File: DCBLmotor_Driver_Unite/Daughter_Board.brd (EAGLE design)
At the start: 107.5 x 78.7 mm, 64 parts, among them CN1 DF11-16DP-2DSA, CN2 26-01-3115, CN3 39-28-1023, IC1 ACS780KLRTR-150B-T, IC2 IR2010SPBF, IC3 IR2010SPBF, IC4 IR2010SPBF, IC5 ACS780KLRTR-150B-T, IC6 ACS780KLRTR-150B-T

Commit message: Version1 per finshed
Per complete Version1
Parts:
- added CN4: (no value), jst-xh:B2B-XH-A
- added PMC4: 50ST104MA13216, Rubycon:3216
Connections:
- new net N$31: DC-DC1.P$6, PMC4.P$1
- net +20V: now also CN4.1
- net GND: now also CN4.2, PMC4.P$2
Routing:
- net GND: track 439.8 -> 447.6 mm
- net CU1: track 60.3 -> 65.8 mm
- net N$31: track 0.00 -> 1.83 mm
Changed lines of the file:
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@@
 <element name="R8" library="ROHM" package="MCR03" value="MCR03" x="88.62554375" y="15.636859375" rot="R180"/>
 <element name="D1" library="DIODE" package="SOD123" value="1N5711W-7-F" x="81.7" y="16.5" rot="R180"/>
+<element name="PMC4" library="Rubycon" package="3216" value="50ST104MA13216" x="89.5" y="19.8"/>
+<element name="CN4" library="jst-xh" package="B2B-XH-A" value="" x="0.8" y="-4.4"/>
 </elements>
 <signals>
@@
 <wire x1="90.099634375" y1="29.800365625" x2="87.4" y2="32.5" width="3" layer="1"/>
 <wire x1="84.8" y1="13.3" x2="92.9" y2="13.3" width="3" layer="1"/>
-<wire x1="96.917065625" y1="17.317065625" x2="96.917065625" y2="23.163078125" width="3" layer="1"/>
+<wire x1="96.917065625" y1="17.317065625" x2="96.917065625" y2="19.8" width="3" layer="1"/>
+<wire x1="96.917065625" y1="19.8" x2="96.917065625" y2="23.163078125" width="3" layer="1"/>
 <wire x1="92.9" y1="13.3" x2="96.917065625" y2="17.317065625" width="3" layer="1"/>
 <wire x1="96.917065625" y1="23.163078125" x2="92.590071875" y2="27.490071875" width="3" layer="1"/>
@@
 <wire x1="84.279053125" y1="30.466625" x2="87.25560625" y2="27.490071875" width="3" layer="1"/>
 <wire x1="87.25560625" y1="27.490071875" x2="92.590071875" y2="27.490071875" width="3" layer="1"/>
+<contactref element="PMC4" pad="P$2"/>
+<wire x1="92.7" y1="19.8" x2="94.9" y2="19.8" width="1.016" layer="1"/>
+<wire x1="94.9" y1="19.8" x2="96.917065625" y2="19.8" width="1.016" layer="1"/>
+<wire x1="94.9" y1="19.8" x2="96.2" y2="18.5" width="1.016" layer="1"/>
+<wire x1="94.9" y1="19.8" x2="96.1" y2="21" width="1.016" layer="1"/>
+<contactref element="CN4" pad="2"/>
 <wire x1="25.7" y1="66.472175" x2="25.814715625" y2="66.76835" width="0" layer="19" extent="16-16"/>
 <wire x1="25.618125" y1="33.3421125" x2="25.618125" y2="33.342115625" width="0" layer="19" extent="16-16"/>
+<wire x1="2.05" y1="-4.4" x2="19.5" y2="20.3" width="0" layer="19" extent="16-16"/>
 </signal>
 <signal name="N$1">
@@
 <wire x1="18.3" y1="37.2" x2="15.4" y2="34.3" width="0.2" layer="1"/>
 <wire x1="13.9" y1="34.3" x2="15.4" y2="34.3" width="0.2" layer="1"/>
-<wire x1="7.6" y1="31.5" x2="9.1" y2="33" width="0.15" layer="1"/>
-<wire x1="9.1" y1="33" x2="12.5" y2="33" width="0.15" layer="1"/>
-<wire x1="12.5" y1="33" x2="13.8" y2="34.3" width="0.15" layer="1"/>
-<wire x1="13.8" y1="34.3" x2="13.9" y2="34.3" width="0.15" layer="1"/>
+<wire x1="7.65" y1="31.55" x2="9.1" y2="33" width="0.15" layer="1"/>
+<wire x1="13.9" y1="34.3" x2="13.8" y2="34.3" width="0.15" layer="1"/>
+<wire x1="7.6" y1="31.5" x2="7.65" y2="31.55" width="0.1524" layer="1"/>
+<wire x1="13.9" y1="34.3" x2="10.4" y2="34.3" width="0.1524" layer="1"/>
+<wire x1="13.8" y1="34.3" x2="10.4" y2="34.3" width="0.2" layer="1"/>
+<wire x1="10.4" y1="34.3" x2="7.65" y2="31.55" width="0.2" layer="1"/>
 <wire x1="29.709803125" y1="71.00635" x2="29.709815625" y2="71.006359375" width="0" layer="19" extent="16-16"/>
 </signal>
@@
 <wire x1="90.099634375" y1="44.531209375" x2="90.099634375" y2="48.900365625" width="3" layer="1"/>
 <wire x1="90.099634375" y1="48.900365625" x2="85.9" y2="53.1" width="3" layer="1"/>
+<contactref element="CN4" pad="1"/>
+<wire x1="-0.45" y1="-4.4" x2="70.5" y2="28.7" width="0" layer="19" extent="16-16"/>
 </signal>
 <signal name="VCC">
@@
 <wire x1="85.840809375" y1="16.614103125" x2="85.840809375" y2="16.61410625" width="0" layer="19" extent="1-1"/>
 </signal>
+<signal name="N$31">
+<contactref element="DC-DC1" pad="P$6"/>
+<contactref element="PMC4" pad="P$1"/>
+<wire x1="89.5" y1="19.8" x2="87.712428125" y2="19.8" width="1.016" layer="1"/>
+<wire x1="87.712428125" y1="19.8" x2="87.679053125" y2="19.766625" width="1.016" layer="1"/>
+</signal>
 </signals>

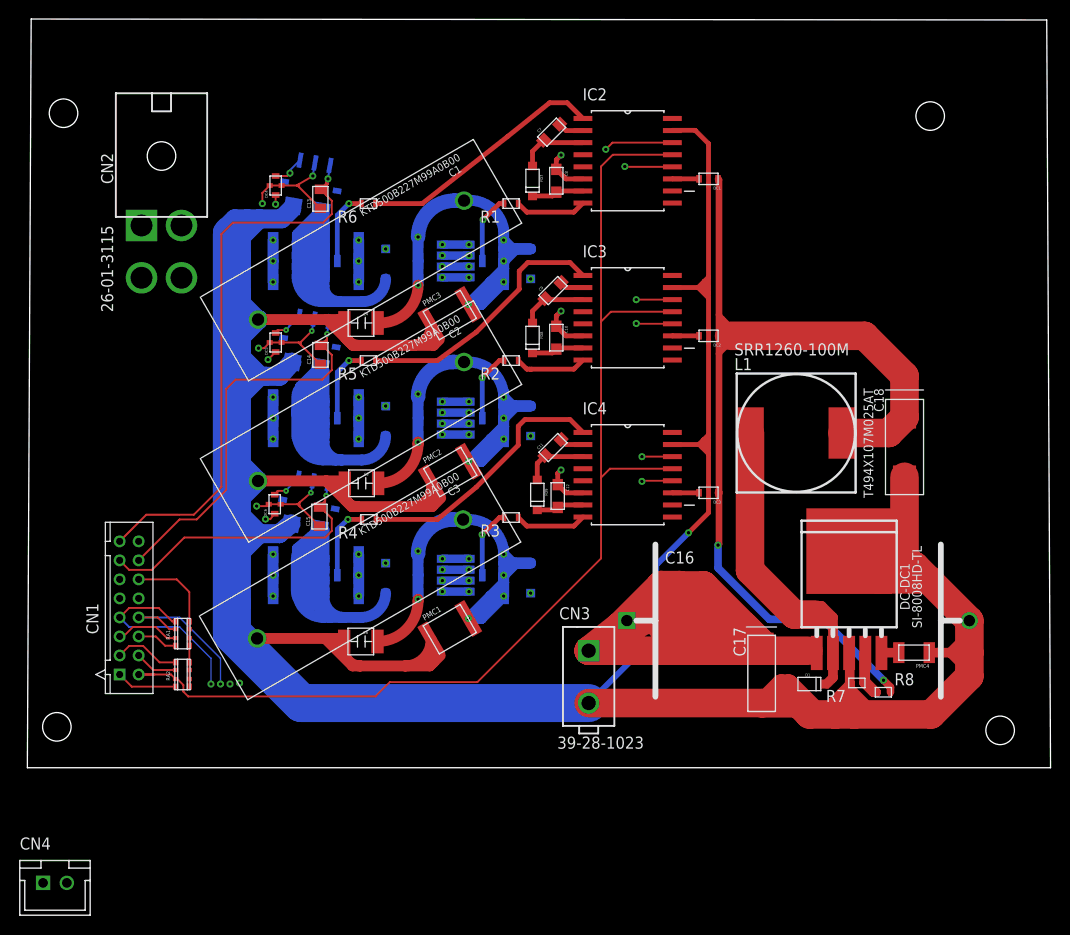
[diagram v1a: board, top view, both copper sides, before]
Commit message: Fix
Add coment in silk
rerote some line
fix External form
Add screw hole
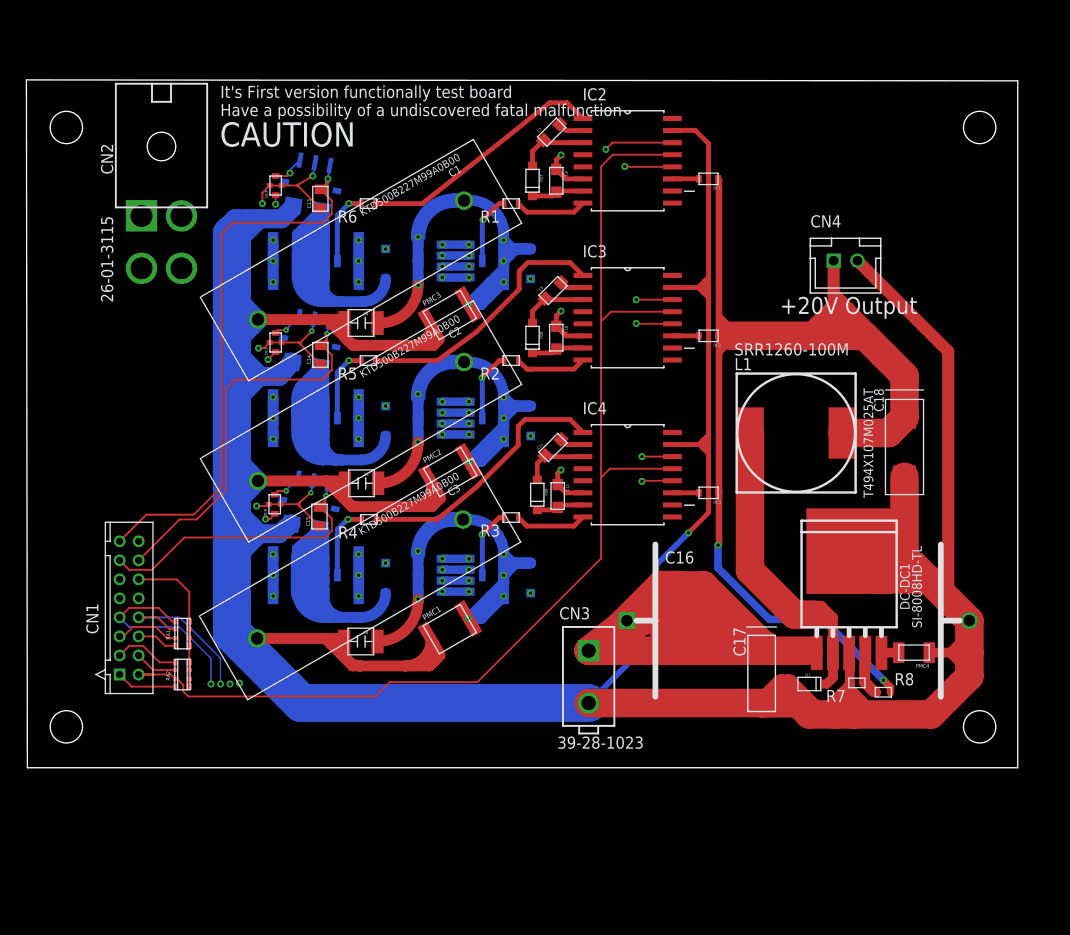
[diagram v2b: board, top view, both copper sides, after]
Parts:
- moved CN4 105.7 mm to (83.9, 61.0)
- moved CN2 1.00 mm to (12.0, 65.7)
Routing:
- net GND: track 447.6 -> 490.3 mm
- net +20V: track 104.1 -> 135.4 mm
- net VS2: track 111.6 -> 112.6 mm
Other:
- board size 107.5 x 78.7 mm -> 104.2 x 72.3 mm
- board text added: "+20V Output"
- board text added: "CAUTION"
- board text added: "It's First version functionally test board Have a possibility of a undiscovered fatal malfunction"
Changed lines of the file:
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@@
 <setting verticaltext="up"/>
 </settings>
-<grid distance="0.1" unitdist="mm" unit="mm" style="lines" multiple="1" display="no" altdistance="5" altunitdist="mil" altunit="mm"/>
+<grid distance="1" unitdist="mm" unit="mm" style="lines" multiple="1" display="no" altdistance="5" altunitdist="mil" altunit="mm"/>
 <layers>
 <layer number="1" name="Top" color="4" fill="1" visible="yes" active="yes"/>
@@
 <board>
 <plain>
-<wire x1="-2.1" y1="7.7" x2="105.45" y2="7.7" width="0" layer="20"/>
-<wire x1="105.45" y1="7.7" x2="105.05" y2="86.3" width="0" layer="20"/>
-<wire x1="105.05" y1="86.3" x2="-1.7" y2="86.4" width="0" layer="20"/>
-<wire x1="-1.7" y1="86.4" x2="-2.1" y2="7.7" width="0" layer="20"/>
-<hole x="1.7" y="76.5" drill="3"/>
-<hole x="92.8" y="76.2" drill="3"/>
-<hole x="100.15179375" y="11.63115" drill="3"/>
-<hole x="1" y="12" drill="3"/>
-<dimension x1="-2.1" y1="7.7" x2="105.45" y2="7.7" x3="51.675" y3="83.4" textsize="1.778" layer="1"/>
-<dimension x1="1" y1="74.9" x2="3.8" y2="7.8" x3="-4.74835625" y3="41.051709375" textsize="1.778" layer="1"/>
+<wire x1="-2.1" y1="7.7" x2="102" y2="7.7" width="0" layer="20"/>
+<wire x1="102" y1="7.7" x2="102" y2="79.9" width="0" layer="20"/>
+<wire x1="102" y1="79.9" x2="-2.2" y2="80" width="0" layer="20"/>
+<wire x1="-2.2" y1="80" x2="-2.1" y2="7.7" width="0" layer="20"/>
+<text x="77" y="55.4" size="1.778" layer="21">+20V Output</text>
+<text x="52.525" y="12.2" size="1.27" layer="22" rot="MR0">It's First version functionally test board
+Have a possibility of a undiscovered fatal malfunction</text>
+<text x="52.575" y="9" size="2.54" layer="22" rot="MR0">CAUTION</text>
+<text x="18.175" y="76.2" size="1.27" layer="21">It's First version functionally test board
+Have a possibility of a undiscovered fatal malfunction</text>
+<text x="18.125" y="73" size="2.54" layer="21">CAUTION</text>
+<hole x="2" y="12" drill="3.4"/>
+<hole x="2" y="75" drill="3.4"/>
+<hole x="98" y="75" drill="3.4"/>
+<hole x="98" y="12" drill="3.4"/>
 </plain>
 <attributes>
@@
 <element name="RA1" library="Pana_Chip_RA" package="EXB-38V,28V" value="EXB-38V103JV" x="14.2" y="21.8" rot="R90"/>
 <element name="RA2" library="Pana_Chip_RA" package="EXB-38V,28V" value="EXB-38V103JV" x="14.2" y="17.5" rot="R90"/>
-<element name="CN2" library="Molex" package="26-01-3115" value="26-01-3115" x="12" y="64.7" rot="R180"/>
+<element name="CN2" library="Molex" package="26-01-3115" value="26-01-3115" x="12" y="65.7" rot="R180"/>
 <element name="CN3" library="Molex" package="39-28-1023" value="39-28-1023" x="56.9" y="20"/>
 <element name="DC-DC1" library="SANKEN" package="D2_PACAGE_5PIN" value="SI-8008HD-TL" x="84.279053125" y="27.466625"/>
@@
 <element name="D1" library="DIODE" package="SOD123" value="1N5711W-7-F" x="81.7" y="16.5" rot="R180"/>
 <element name="PMC4" library="Rubycon" package="3216" value="50ST104MA13216" x="89.5" y="19.8"/>
-<element name="CN4" library="jst-xh" package="B2B-XH-A" value="" x="0.8" y="-4.4"/>
+<element name="CN4" library="jst-xh" package="B2B-XH-A" value="" x="83.9" y="61"/>
 </elements>
 <signals>
@@
 <wire x1="94.9" y1="19.8" x2="96.1" y2="21" width="1.016" layer="1"/>
 <contactref element="CN4" pad="2"/>
+<wire x1="85.15" y1="61" x2="94.7" y2="51.45" width="1.27" layer="1"/>
+<wire x1="94.7" y1="25.38014375" x2="96.917065625" y2="23.163078125" width="1.27" layer="1"/>
+<wire x1="94.7" y1="51.45" x2="94.7" y2="25.38014375" width="1.27" layer="1"/>
 <wire x1="25.7" y1="66.472175" x2="25.814715625" y2="66.76835" width="0" layer="19" extent="16-16"/>
 <wire x1="25.618125" y1="33.3421125" x2="25.618125" y2="33.342115625" width="0" layer="19" extent="16-16"/>
-<wire x1="2.05" y1="-4.4" x2="19.5" y2="20.3" width="0" layer="19" extent="16-16"/>
 </signal>
 <signal name="N$1">
@@
 <wire x1="20.2" y1="60.9" x2="23.67" y2="60.9" width="4" layer="3"/>
 <wire x1="23.67" y1="60.9" x2="23.73" y2="60.96" width="4" layer="3"/>
-<wire x1="14.1" y1="64.7" x2="16.4" y2="64.7" width="3.5" layer="3"/>
+<wire x1="14.1" y1="65.7" x2="16.4" y2="64.7" width="3.5" layer="3"/>
 <wire x1="53.499996875" y1="70.6" x2="53.5" y2="70.6" width="0" layer="19" extent="1-1"/>
 </signal>
@@
 <wire x1="9.9" y1="57.3" x2="22.75" y2="44.45" width="4" layer="3"/>
 <wire x1="22.75" y1="44.45" x2="23.73" y2="44.45" width="4" layer="3"/>
-<wire x1="9.9" y1="59.2" x2="9.9" y2="57.3" width="3.5" layer="3"/>
+<wire x1="9.9" y1="60.2" x2="9.9" y2="57.3" width="3.5" layer="3"/>
 </signal>
 <signal name="VS3">
@@
 <wire x1="54" y1="29.26" x2="50.8" y2="26.06" width="0.508" layer="3"/>
 <contactref element="CN2" pad="P$1"/>
-<wire x1="9.9" y1="64.7" x2="8.7" y2="64.7" width="3.5" layer="3"/>
+<wire x1="9.9" y1="65.7" x2="8.7" y2="64.7" width="3.5" layer="3"/>
 <wire x1="5.2" y1="54.7" x2="17.6" y2="42.3" width="4" layer="3"/>
 <wire x1="17.6" y1="42.3" x2="17.6" y2="34.07" width="4" layer="3"/>
@@
 <wire x1="71" y1="54.9" x2="71" y2="53.9" width="0.508" layer="1"/>
 <wire x1="71" y1="53.9" x2="71.8" y2="53.1" width="0.508" layer="1"/>
-<wire x1="85.9" y1="53.1" x2="71.8" y2="53.1" width="3" layer="1"/>
+<wire x1="85.9" y1="53.1" x2="83.4" y2="53.1" width="3" layer="1"/>
 <contactref element="C18" pad="P$+"/>
+<wire x1="83.4" y1="53.1" x2="81.1" y2="53.1" width="3" layer="1"/>
+<wire x1="81.1" y1="53.1" x2="71.8" y2="53.1" width="3" layer="1"/>
 <wire x1="83.55994375" y1="42.88495625" x2="88.45338125" y2="42.88495625" width="3" layer="1"/>
 <wire x1="88.45338125" y1="42.88495625" x2="90.099634375" y2="44.531209375" width="3" layer="1"/>
 <wire x1="90.099634375" y1="44.531209375" x2="90.099634375" y2="48.900365625" width="3" layer="1"/>
-<wire x1="90.099634375" y1="48.900365625" x2="85.9" y2="53.1" width="3" layer="1"/>
+<wire x1="90.099634375" y1="48.900365625" x2="88.05" y2="50.95" width="3" layer="1"/>
 <contactref element="CN4" pad="1"/>
-<wire x1="-0.45" y1="-4.4" x2="70.5" y2="28.7" width="0" layer="19" extent="16-16"/>
+<wire x1="88.05" y1="50.95" x2="85.9" y2="53.1" width="3" layer="1"/>
+<wire x1="82.65" y1="61" x2="82.65" y2="57.55" width="1.27" layer="1"/>
+<wire x1="82.65" y1="57.55" x2="83.55" y2="56.65" width="1.27" layer="1"/>
+<wire x1="83.55" y1="56.65" x2="84.15" y2="56.05" width="1.27" layer="1"/>
+<wire x1="84.15" y1="56.05" x2="87.3" y2="52.9" width="1.27" layer="1"/>
+<wire x1="87.3" y1="52.9" x2="87.3" y2="50.8" width="1.27" layer="1"/>
+<wire x1="88.1" y1="50" x2="87.3" y2="50.8" width="1.27" layer="1"/>
+<wire x1="88.05" y1="50.95" x2="88.1" y2="50.9" width="1.27" layer="1"/>
+<wire x1="88.1" y1="50.9" x2="88.1" y2="50" width="1.27" layer="1"/>
+<wire x1="85.9" y1="53.1" x2="84.15" y2="54.85" width="1.27" layer="1"/>
+<wire x1="84.15" y1="54.85" x2="84.15" y2="56.05" width="1.27" layer="1"/>
+<wire x1="83.4" y1="53.1" x2="83.4" y2="56.5" width="1.27" layer="1"/>
+<wire x1="83.4" y1="56.5" x2="83.55" y2="56.65" width="1.27" layer="1"/>
+<wire x1="82.65" y1="57.55" x2="82.65" y2="56.4" width="1.27" layer="1"/>
+<wire x1="82.65" y1="56.4" x2="82.65" y2="54.7" width="1.27" layer="1"/>
+<wire x1="82.65" y1="54.65" x2="82.65" y2="53.95" width="1.27" layer="1"/>
+<wire x1="82.65" y1="53.95" x2="82.5" y2="53.8" width="1.27" layer="1"/>
+<wire x1="82.65" y1="56.4" x2="80" y2="53.75" width="1.27" layer="1"/>
+<wire x1="80" y1="53.75" x2="80" y2="53.7" width="1.27" layer="1"/>
+<wire x1="81.1" y1="53.1" x2="82.65" y2="54.65" width="1.27" layer="1"/>
+<wire x1="82.65" y1="54.65" x2="82.65" y2="54.7" width="1.27" layer="1"/>
 </signal>
 <signal name="VCC">
@@
 </board>
 </drawing>
+<compatibility>
+<note version="6.3" minversion="6.2.2" severity="warning">
+Since Version 6.2.2 text objects can contain more than one line,
+which will not be processed correctly with this version.
+</note>
+</compatibility>
 </eagle>

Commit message: Assigned Parts No.
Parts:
- added R10, R11, R12, R13, R14, R9: ESR03EZPJ753, ROHM:ESR03
- DC1, DC2, DC3, DC4, DC5, DC6: value YFF21PC -> YFF21PC1E104MT000N
- R1, R2, R3, R4, R5, R6: value MCR03 -> ESR03EZPJ102; device ROHM:MCR03 -> ROHM:ESR03
- R7: value MCR03 -> RN55C8000BB14; device ROHM:MCR03 -> VISHAY:CMF55
- R8: value MCR03 -> RN55C1912BB14; device ROHM:MCR03 -> VISHAY:CMF55
- moved R7 9.50 mm to (93.2, 13.1), turned to 90 degrees
- moved R4 4.00 mm to (37.0, 33.8)
- moved R5 4.00 mm to (37.0, 50.5)
- moved R6 4.00 mm to (37.0, 67.0)
- moved R8 2.50 mm to (89.0, 13.2), turned to 90 degrees
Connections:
- removed net N$2: C11.P$1, IC4.2
- removed net N$22: C7.P$2, FD7.A, IC2.3
- removed net N$24: C9.P$2, FD8.A, IC3.3
- removed net N$26: C11.P$2, FD9.A, IC4.3
- removed net N$4: C9.P$1, IC3.2
- removed net N$6: C7.P$1, IC2.2
- net +20V: now also C11.P$2, C7.P$2, C9.P$2, FD7.A, FD8.A, FD9.A, IC2.3, IC3.3, IC4.3
- net GND: now also C11.P$1, C7.P$1, C9.P$1, IC2.2, IC3.2, IC4.2
- net N$14: now also R13.P$1
- net N$15: now also R12.P$2
- net N$18: now also R12.P$1
- net N$19: now also R11.P$1
- net N$20: now also R10.P$1
- net N$21: now also R9.P$1
- net N$3: now also R14.P$2
- net N$5: now also R13.P$2
- net N$9: now also R14.P$1
- net VS1: now also R9.P$2
- net VS2: now also R10.P$2
- net VS3: now also R11.P$2
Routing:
- net GND: track 490.3 -> 535.1 mm
- net +20V: track 135.4 -> 168.7 mm, vias 2 -> 4
- net N$22: track 7.43 -> 0.00 mm
- net N$24: track 7.14 -> 0.00 mm
- net N$26: track 6.93 -> 0.00 mm
- net N$9: track 7.85 -> 11.1 mm
- net N$18: track 7.80 -> 11.1 mm
- net N$14: track 7.86 -> 11.1 mm
- net LO3: track 27.7 -> 24.4 mm
- net LO2: track 27.5 -> 24.2 mm
- net LO1: track 26.2 -> 22.9 mm
- net N$6: track 2.73 -> 0.00 mm
- net N$4: track 2.52 -> 0.00 mm
- net N$2: track 2.52 -> 0.00 mm
- net HO3: track 7.57 -> 8.18 mm
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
